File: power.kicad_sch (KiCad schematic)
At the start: 27 parts, among them IC5 BQ24074RGTR, IC6 LP2985-30DBVR, IC7 NCP718ASN300T1G, IC8 MPM3833CGRH-Z, J4 217175-0001, U2 NC7SVU04P5X

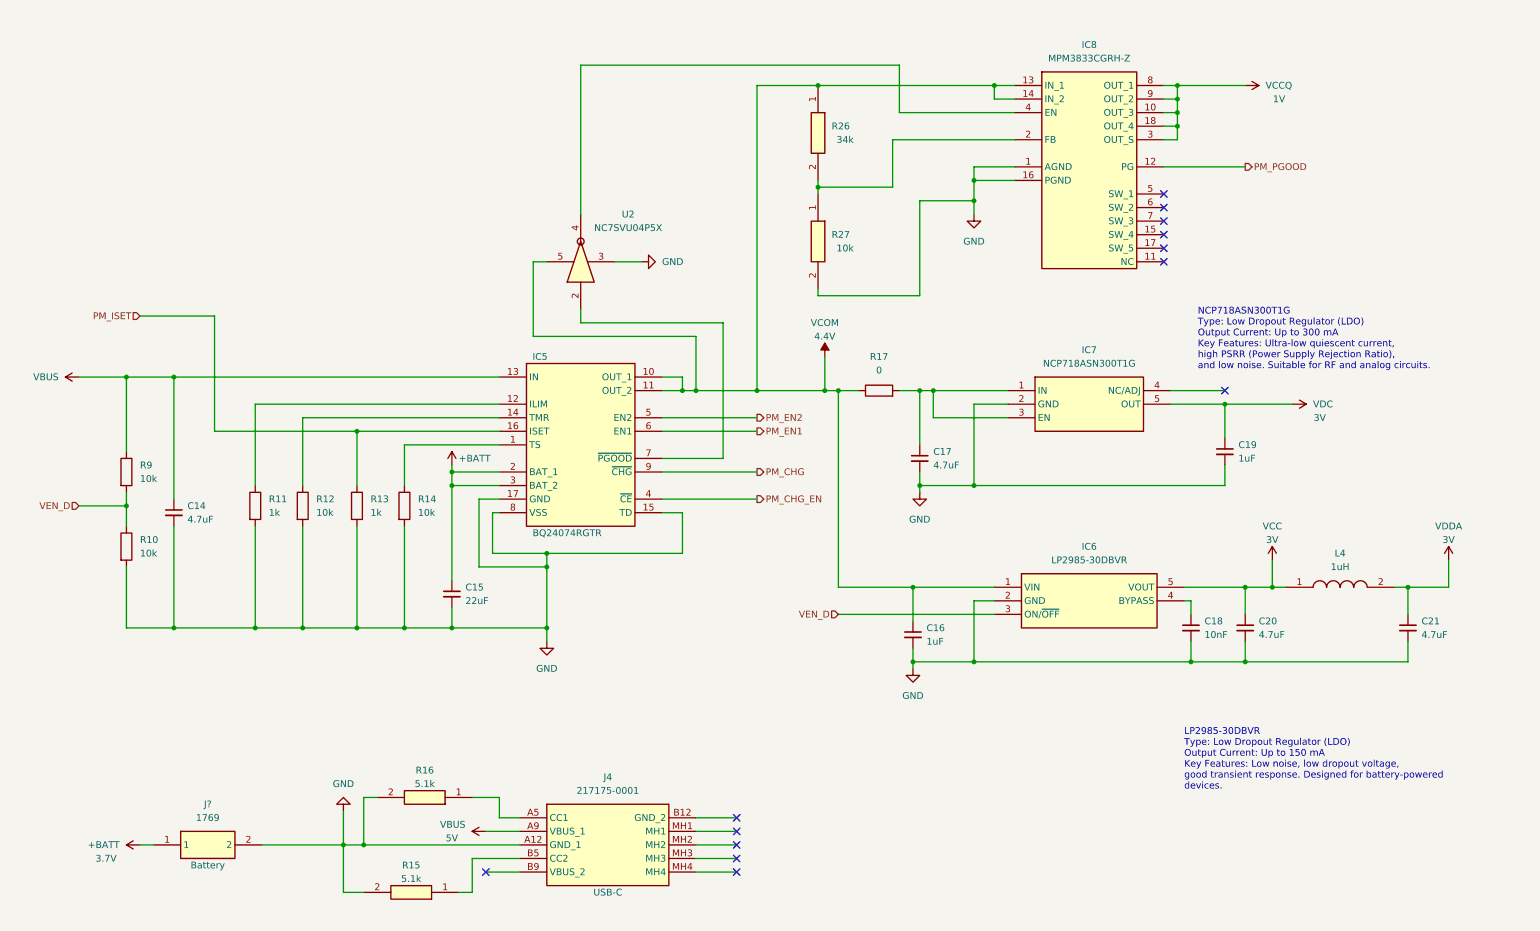
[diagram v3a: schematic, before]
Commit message: Moved USB-C connector to root sheet
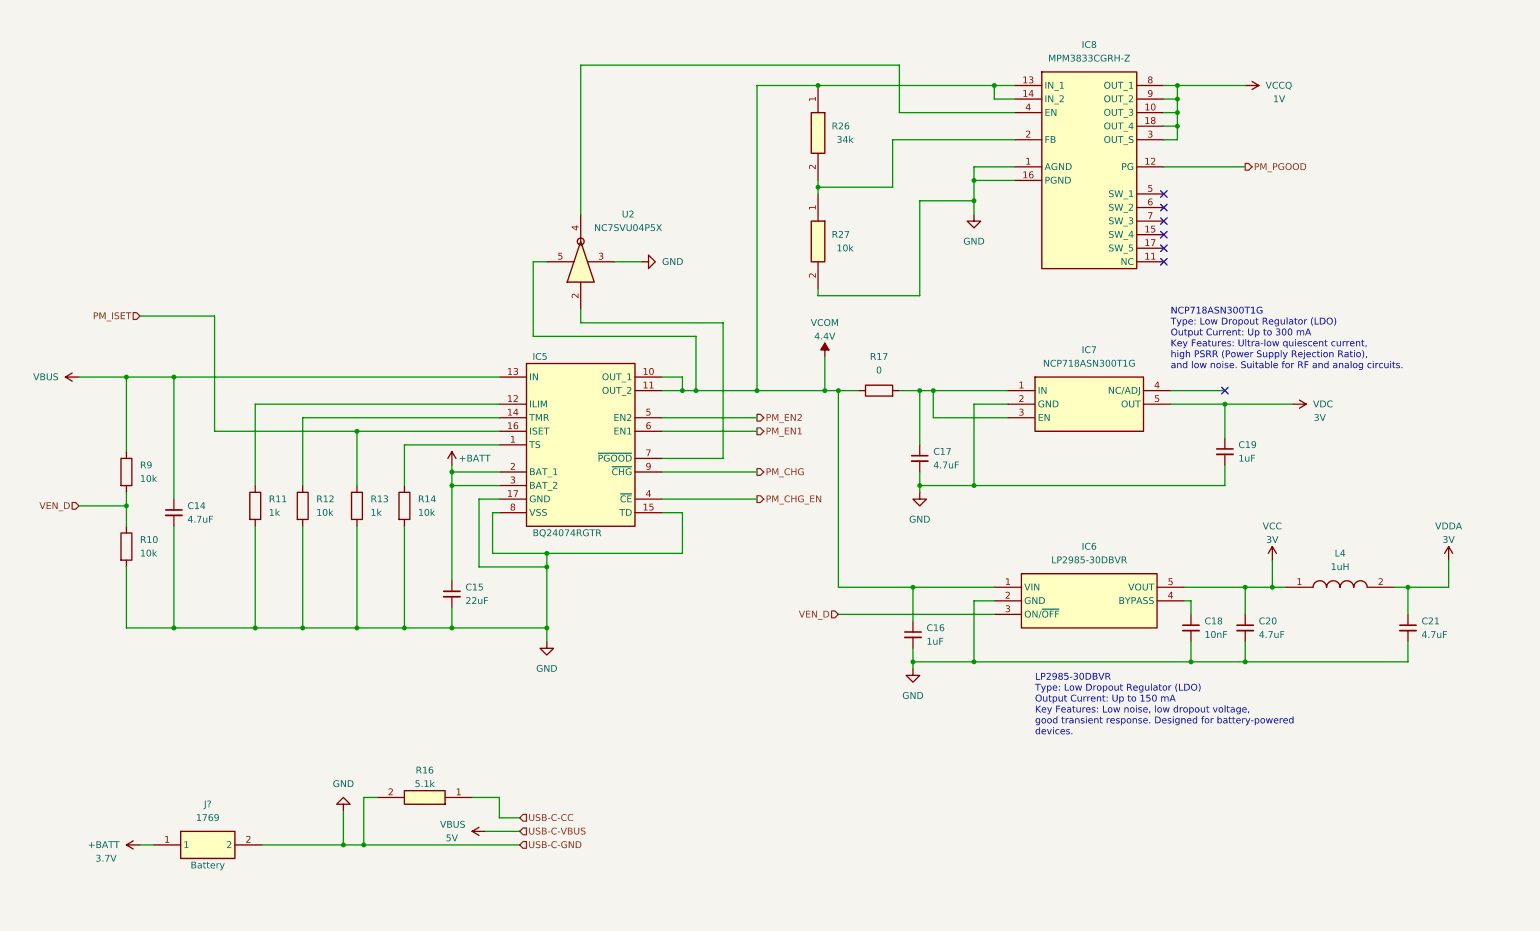
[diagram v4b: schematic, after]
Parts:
- removed J4: 217175-0001, 2171750001, symbol SamacSys_Parts:217175-0001
- removed R15: CRCW04025K10FKTD, RESC1005X40N, symbol SamacSys_Parts:CRCW04025K10FKTD
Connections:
- net USB-C-CC: now reaches R16.1
- no-connect marks 13 -> 7
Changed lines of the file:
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@@
   (junction (at 151.13 87.63) (diameter 0) (color 0 0 0 0)
   )
-  (no_connect (at 147.32 175.26))
   (no_connect (at 227.33 58.42))
   (no_connect (at 227.33 60.96))
-  (no_connect (at 147.32 177.8))
   (no_connect (at 227.33 53.34))
-  (no_connect (at 147.32 170.18))
   (no_connect (at 227.33 55.88))
   (no_connect (at 227.33 63.5))
   (no_connect (at 227.33 50.8))
-  (no_connect (at 147.32 172.72))
-  (no_connect (at 100.33 177.8))
   (no_connect (at 238.76 87.63))
-  (no_connect (at 147.32 167.64))
   (wire (pts (xy 93.98 128.27) (xy 93.98 132.08))
     (stroke (width 0) (type default))
@@
     (stroke (width 0) (type default))
   )
-  (wire (pts (xy 100.33 177.8) (xy 106.68 177.8))
-    (stroke (width 0) (type default))
-  )
   (wire (pts (xy 144.78 74.93) (xy 144.78 100.33))
     (stroke (width 0) (type default))
@@
     (stroke (width 0) (type default))
   )
-  (wire (pts (xy 97.79 181.61) (xy 95.25 181.61))
-    (stroke (width 0) (type default))
-  )
   (wire (pts (xy 242.57 124.46) (xy 242.57 129.54))
     (stroke (width 0) (type default))
@@
     (stroke (width 0) (type default))
   )
-  (wire (pts (xy 139.7 175.26) (xy 147.32 175.26))
-    (stroke (width 0) (type default))
-  )
   (wire (pts (xy 93.98 101.6) (xy 93.98 102.87))
     (stroke (width 0) (type default))
@@
     (stroke (width 0) (type default))
   )
-  (wire (pts (xy 139.7 172.72) (xy 147.32 172.72))
-    (stroke (width 0) (type default))
-  )
   (wire (pts (xy 151.13 87.63) (xy 163.83 87.63))
     (stroke (width 0) (type default))
@@
     (stroke (width 0) (type default))
   )
-  (wire (pts (xy 97.79 175.26) (xy 106.68 175.26))
-    (stroke (width 0) (type default))
-  )
   (wire (pts (xy 109.22 77.47) (xy 109.22 63.5))
     (stroke (width 0) (type default))
@@
     (stroke (width 0) (type default))
   )
-  (wire (pts (xy 139.7 167.64) (xy 147.32 167.64))
-    (stroke (width 0) (type default))
-  )
   (wire (pts (xy 118.11 26.67) (xy 177.8 26.67))
     (stroke (width 0) (type default))
@@
     (stroke (width 0) (type default))
   )
-  (wire (pts (xy 139.7 170.18) (xy 147.32 170.18))
-    (stroke (width 0) (type default))
-  )
   (wire (pts (xy 76.2 113.03) (xy 76.2 132.08))
     (stroke (width 0) (type default))
@@
     (stroke (width 0) (type default))
   )
-  (wire (pts (xy 139.7 177.8) (xy 147.32 177.8))
-    (stroke (width 0) (type default))
-  )
   (wire (pts (xy 137.16 85.09) (xy 137.16 87.63))
     (stroke (width 0) (type default))
@@
     (stroke (width 0) (type default))
   )
-  (wire (pts (xy 73.66 181.61) (xy 77.47 181.61))
-    (stroke (width 0) (type default))
-  )
   (wire (pts (xy 273.05 134.62) (xy 273.05 138.43))
     (stroke (width 0) (type default))
@@
     (stroke (width 0) (type default))
   )
-  (wire (pts (xy 97.79 181.61) (xy 97.79 175.26))
-    (stroke (width 0) (type default))
-  )
   (wire (pts (xy 99.06 107.95) (xy 99.06 120.65))
     (stroke (width 0) (type default))
@@
     (stroke (width 0) (type default))
   )
-  (wire (pts (xy 73.66 181.61) (xy 73.66 172.72))
-    (stroke (width 0) (type default))
-  )
   (wire (pts (xy 139.7 87.63) (xy 151.13 87.63))
     (stroke (width 0) (type default))
@@
   )
   (text "NCP718ASN300T1G\nType: Low Dropout Regulator (LDO)\nOutput Current: Up to 300 mA\nKey Features: Ultra-low quiescent current, \nhigh PSRR (Power Supply Rejection Ratio), \nand low noise. Suitable for RF and analog circuits."
-    (at 233.68 83.82 0)
+    (at 228.6 83.82 0)
     (effects (font (size 1.27 1.27)) (justify left bottom))
   )
   (text "LP2985-30DBVR\nType: Low Dropout Regulator (LDO)\nOutput Current: Up to 150 mA\nKey Features: Low noise, low dropout voltage,\ngood transient response. Designed for battery-powered\ndevices."
-    (at 231.14 162.56 0)
+    (at 203.2 152.4 0)
     (effects (font (size 1.27 1.27)) (justify left bottom))
+  )
+  (hierarchical_label "USB-C-GND" (shape input) (at 106.68 172.72 0) (fields_autoplaced)
+    (effects (font (size 1.27 1.27)) (justify left))
   )
   (hierarchical_label "PM_EN1" (shape output) (at 151.13 95.25 0) (fields_autoplaced)
@@
   )
   (hierarchical_label "PM_EN2" (shape output) (at 151.13 92.71 0) (fields_autoplaced)
+    (effects (font (size 1.27 1.27)) (justify left))
+  )
+  (hierarchical_label "USB-C-CC" (shape input) (at 106.68 167.64 0) (fields_autoplaced)
+    (effects (font (size 1.27 1.27)) (justify left))
+  )
+  (hierarchical_label "USB-C-VBUS" (shape input) (at 106.68 170.18 0) (fields_autoplaced)
     (effects (font (size 1.27 1.27)) (justify left))
   )
@@
         (path "/de6644e7-b724-4f9d-a608-dcd90a915848"
           (reference "J?") (unit 1)
-        )
-      )
-    )
-  )
-  (symbol (lib_id "SamacSys_Parts:CRCW04025K10FKTD") (at 95.25 181.61 180) (unit 1)
-    (in_bom yes) (on_board yes) (dnp no)
-    (property "Reference" "R15" (at 86.36 176.53 0)
-      (effects (font (size 1.27 1.27)))
-    )
-    (property "Value" "CRCW04025K10FKTD" (at 86.36 177.8 0)
-      (effects (font (size 1.27 1.27)) hide)
-    )
-    (property "Footprint" "RESC1005X40N" (at 81.28 85.42 0)
-      (effects (font (size 1.27 1.27)) (justify left top) hide)
-    )
-    (property "Datasheet" "http://www.vishay.com/docs/20035/dcrcwe3.pdf" (at 81.28 -14.58 0)
-      (effects (font (size 1.27 1.27)) (justify left top) hide)
-    )
-    (property "Height" "0.4" (at 81.28 -214.58 0)
-      (effects (font (size 1.27 1.27)) (justify left top) hide)
-    )
-    (property "Mouser Part Number" "71-CRCW0402-5.1K" (at 81.28 -314.58 0)
-      (effects (font (size 1.27 1.27)) (justify left top) hide)
-    )
-    (property "Mouser Price/Stock" "https://www.mouser.co.uk/ProductDetail/Vishay-Dale/CRCW04025K10FKTD?qs=tEoI2WxJuYtWUw7PHRiLkg%3D%3D" (at 81.28 -414.58 0)
-      (effects (font (size 1.27 1.27)) (justify left top) hide)
-    )
-    (property "Manufacturer_Name" "Vishay" (at 81.28 -514.58 0)
-      (effects (font (size 1.27 1.27)) (justify left top) hide)
-    )
-    (property "Manufacturer_Part_Number" "CRCW04025K10FKTD" (at 81.28 -614.58 0)
-      (effects (font (size 1.27 1.27)) (justify left top) hide)
-    )
-    (property "Display" "5.1k" (at 86.36 179.07 0)
-      (effects (font (size 1.27 1.27)))
-    )
-    (pin "1")
-    (pin "2")
-    (instances
-      (project "drone"
-        (path "/a9d9e6e7-8403-4088-be51-8a69908fe001/b6bf16a7-faa7-434f-9005-38b8369fbbd9"
-          (reference "R15") (unit 1)
-        )
-      )
-      (project "POWER"
-        (path "/befccfa1-9d24-4d6c-8c76-8e884d08ff73"
-          (reference "R?") (unit 1)
-        )
-      )
-      (project "drone"
-        (path "/d34d8324-c983-4098-8d7e-5c2fbd34794d/f990703e-099d-439c-9e1d-875871db40e1"
-          (reference "R7") (unit 1)
         )
       )
@@
         )
       )
-    )
-  )
-  (symbol (lib_id "SamacSys_Parts:217175-0001") (at 106.68 167.64 0) (unit 1)
-    (in_bom yes) (on_board yes) (dnp no)
-    (property "Reference" "J4" (at 123.19 160.02 0)
-      (effects (font (size 1.27 1.27)))
-    )
-    (property "Value" "217175-0001" (at 123.19 162.56 0)
-      (effects (font (size 1.27 1.27)))
-    )
-    (property "Footprint" "2171750001" (at 135.89 262.56 0)
-      (effects (font (size 1.27 1.27)) (justify left top) hide)
-    )
-    (property "Datasheet" "https://www.molex.com/pdm_docs/sd/2171750001_sd.pdf" (at 135.89 362.56 0)
-      (effects (font (size 1.27 1.27)) (justify left top) hide)
-    )
-    (property "Height" "3.46" (at 135.89 562.56 0)
-      (effects (font (size 1.27 1.27)) (justify left top) hide)
-    )
-    (property "Mouser Part Number" "538-217175-0001" (at 135.89 662.56 0)
-      (effects (font (size 1.27 1.27)) (justify left top) hide)
-    )
-    (property "Mouser Price/Stock" "https://www.mouser.co.uk/ProductDetail/Molex/217175-0001?qs=DRkmTr78QARWJMiqNnldSg%3D%3D" (at 135.89 762.56 0)
-      (effects (font (size 1.27 1.27)) (justify left top) hide)
-    )
-    (property "Manufacturer_Name" "Molex" (at 135.89 862.56 0)
-      (effects (font (size 1.27 1.27)) (justify left top) hide)
-    )
-    (property "Manufacturer_Part_Number" "217175-0001" (at 135.89 962.56 0)
-      (effects (font (size 1.27 1.27)) (justify left top) hide)
-    )
-    (property "Component" "USB-C" (at 123.19 181.61 0)
-      (effects (font (size 1.27 1.27)))
-    )
-    (pin "A12")
-    (pin "A5")
-    (pin "A9")
-    (pin "B12")
-    (pin "B5")
-    (pin "B9")
-    (pin "MH1")
-    (pin "MH2")
-    (pin "MH3")
-    (pin "MH4")
-    (instances
-      (project "drone"
-        (path "/a9d9e6e7-8403-4088-be51-8a69908fe001/b6bf16a7-faa7-434f-9005-38b8369fbbd9"
-          (reference "J4") (unit 1)
-        )
-      )
-      (project "POWER"
-        (path "/befccfa1-9d24-4d6c-8c76-8e884d08ff73"
-          (reference "J?") (unit 1)
-        )
-      )
-      (project "drone"
-        (path "/d34d8324-c983-4098-8d7e-5c2fbd34794d/f990703e-099d-439c-9e1d-875871db40e1"
-          (reference "J2") (unit 1)
-        )
-      )

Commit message: Removed RF module for now
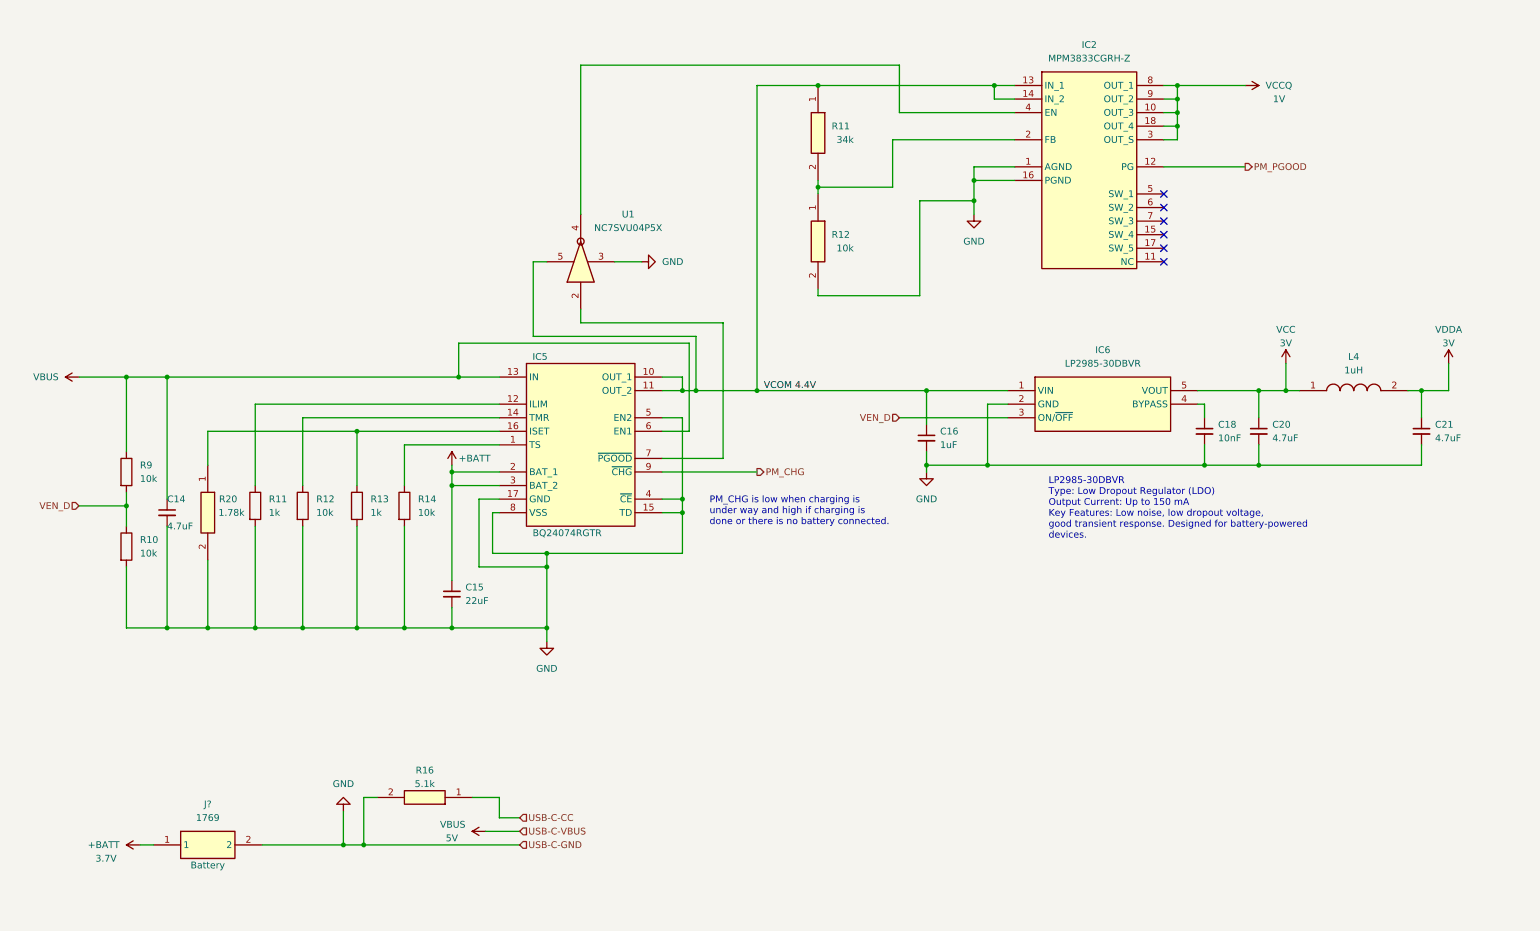
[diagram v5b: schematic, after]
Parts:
- removed C17: 4.7uF_1206_lowESR, 4ms_Capacitor:C_1206, symbol PCM_4ms_Capacitor:4.7uF_1206_lowESR
- removed C19: 1uF_0603_25V, 4ms_Capacitor:C_0603, symbol PCM_4ms_Capacitor:1uF_0603_25V
- removed IC7: NCP718ASN300T1G, SOT95P280X100-5N, symbol SamacSys_Parts:NCP718ASN300T1G
- removed R17: 0R_0603, 4ms_Resistor:R_0603, symbol PCM_4ms_Resistor:0R_0603
- added R20: ERA-3VEB1781V, ERA3KV_(0603), symbol SamacSys_Parts:ERA-3VEB1781V
- renumbered IC8 to IC2, R26 to R11, R27 to R12, U2 to U1
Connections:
- net PM_CHG_EN is gone; now on net GND: IC5.4 (~{CE})
- net PM_EN1 is gone; now on net VBUS: IC5.6 (EN1)
- net PM_EN2 is gone; now on net GND: IC5.5 (EN2)
- net GND: now also R20.2
- net PM_ISET: no longer names the net of IC5.16 (ISET), R13.1
- net PM_ISET: now also R20.1
- net VCOM renamed VCOM 4.4V
- no-connect marks 7 -> 6
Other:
- note added: "PM_CHG is low when charging is under way and high if charging is done or there is no battery connected."
- note removed: "NCP718ASN300T1G Type: Low Dropout Regulator (LDO) Output Current: Up to 300 mA Key Features: Ultra-low quiescent current, high PSRR (Power Supply Rejection Ratio), and low noise. Suitable for RF and analog circuits."
- moved on the sheet: C14, C16, C18, C20, C21, IC6, L4
